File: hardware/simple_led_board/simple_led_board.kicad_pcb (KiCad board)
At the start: 2 copper layers, 33.6 x 35.6 mm, 3 parts, among them J1 Conn_02x03_Odd_Even

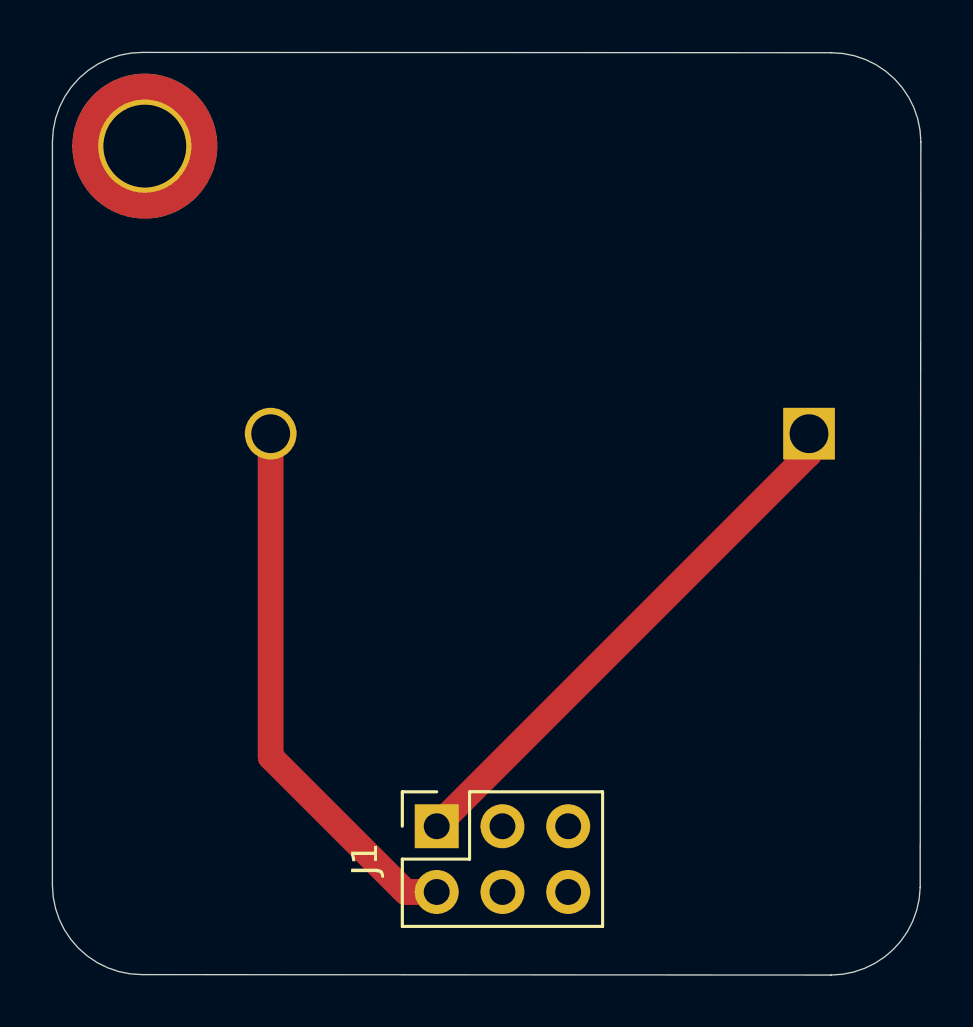
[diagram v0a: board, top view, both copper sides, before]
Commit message: Show hardware check issues as tables
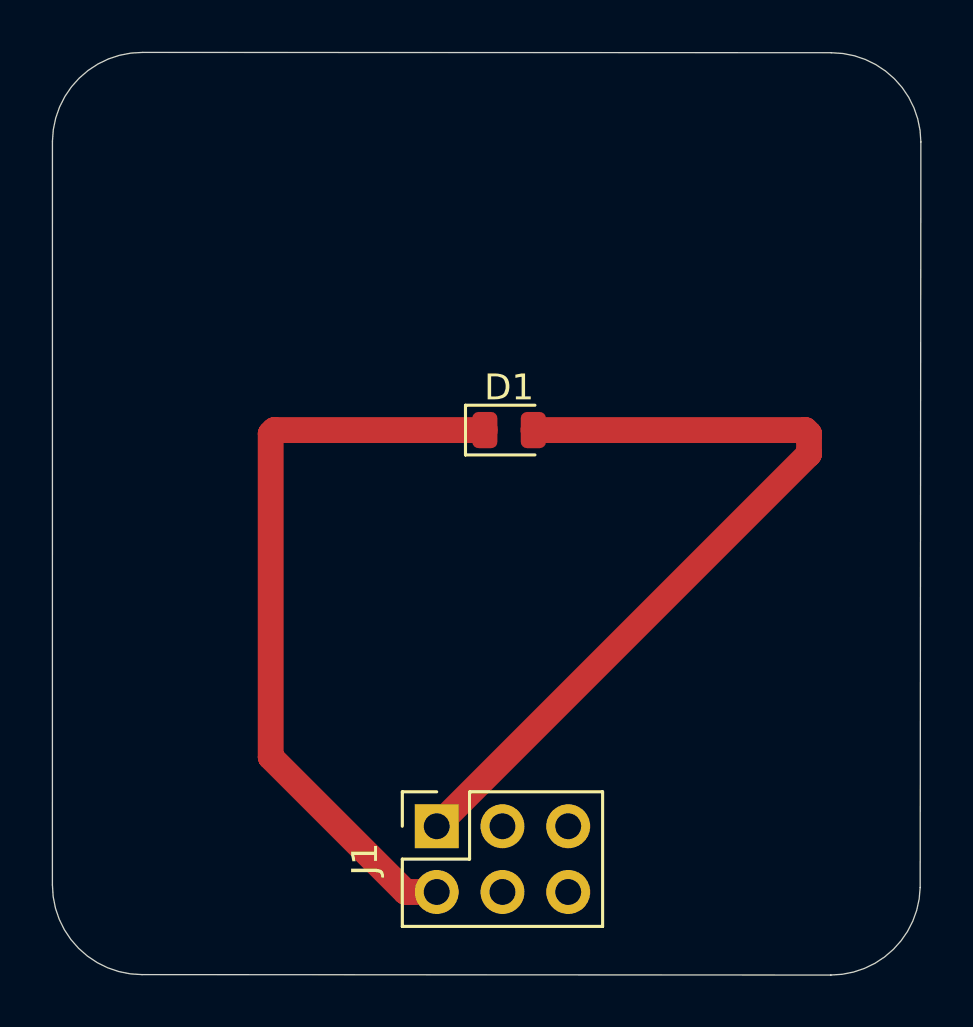
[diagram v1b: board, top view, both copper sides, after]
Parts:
- removed BT1: Battery, Battery:BatteryHolder_MYOUNG_BS-07-A1BJ001_CR2032
- removed REF**: MountingHole_3.2mm_M3_DIN965_Pad_TopBottom, MountingHole:MountingHole_3.2mm_M3_DIN965_Pad_TopBottom
- added D1: LED, LED_SMD:LED_0805_2012Metric, F.Cu at (163.1, 72.5)
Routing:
- net Net-(D1-A): track 24.3 -> 35.0 mm
- net Net-(D1-K): track 21.1 -> 29.4 mm
